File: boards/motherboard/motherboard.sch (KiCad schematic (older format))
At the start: 40 parts, among them J1 RJ45, J2 RJ45, J3 RJ45, J4 RJ45, J5 RJ45, U1 EBAYPCA9685

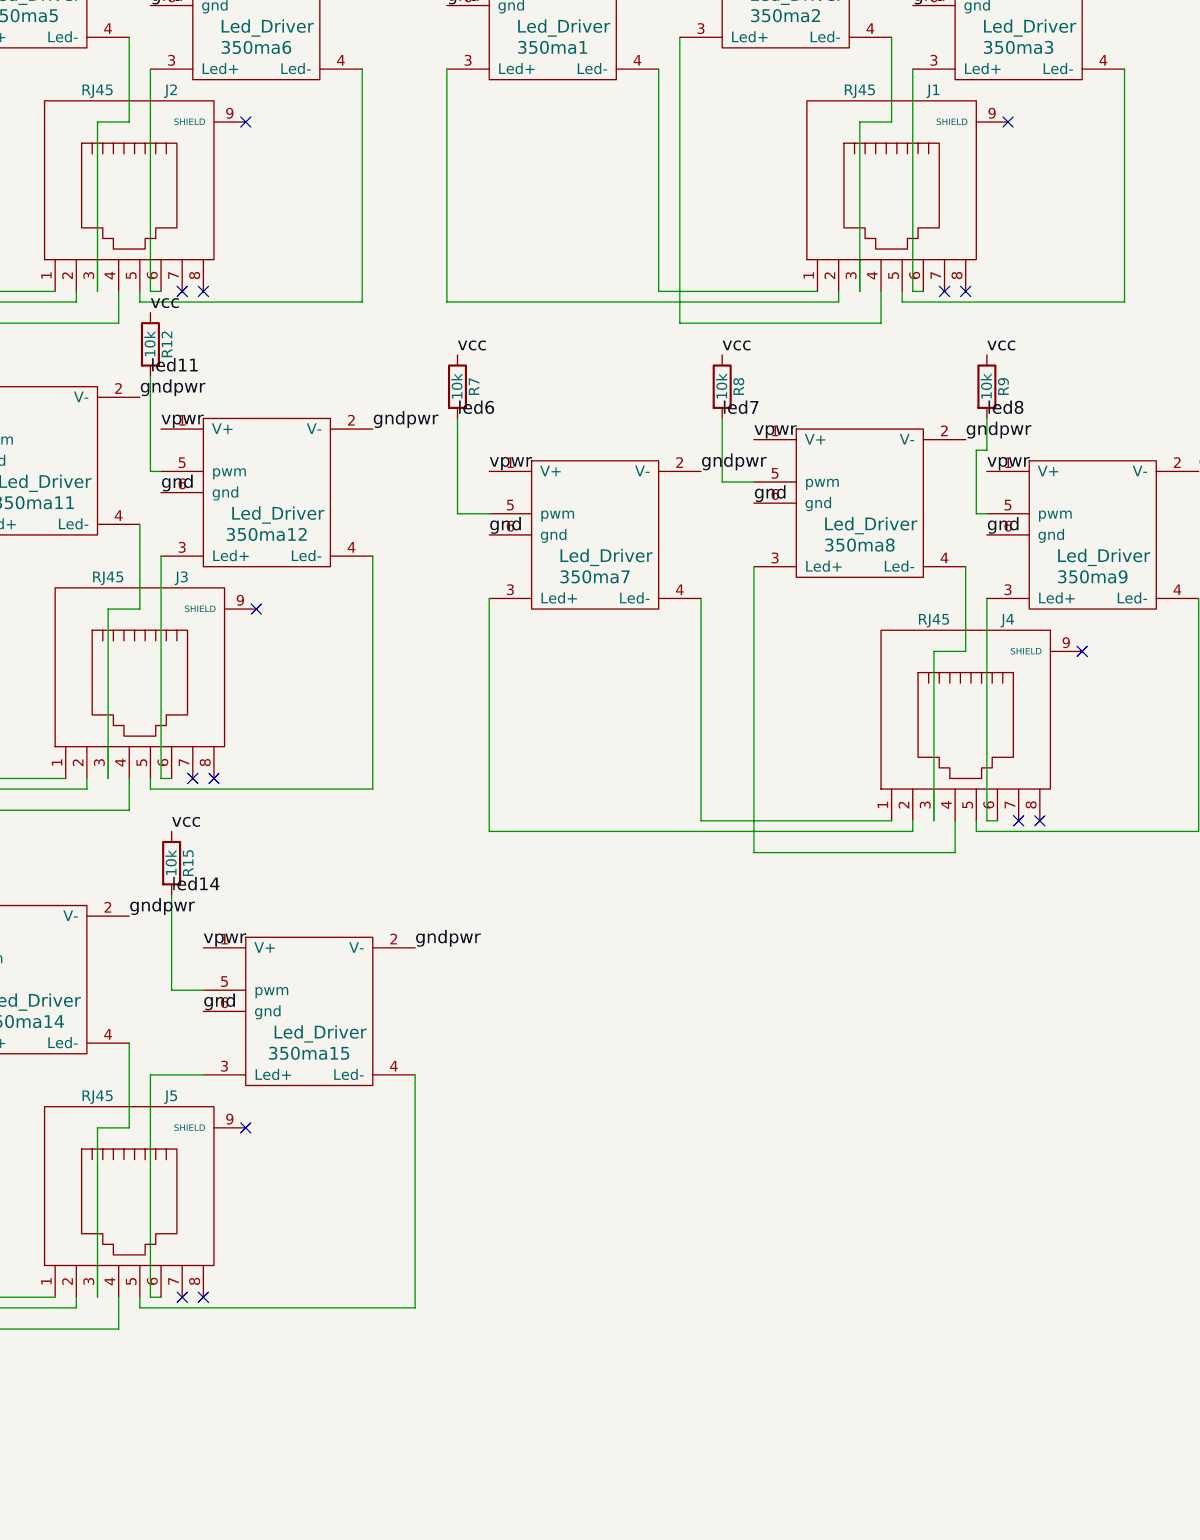
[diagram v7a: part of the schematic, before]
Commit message: added breakout for ethernet
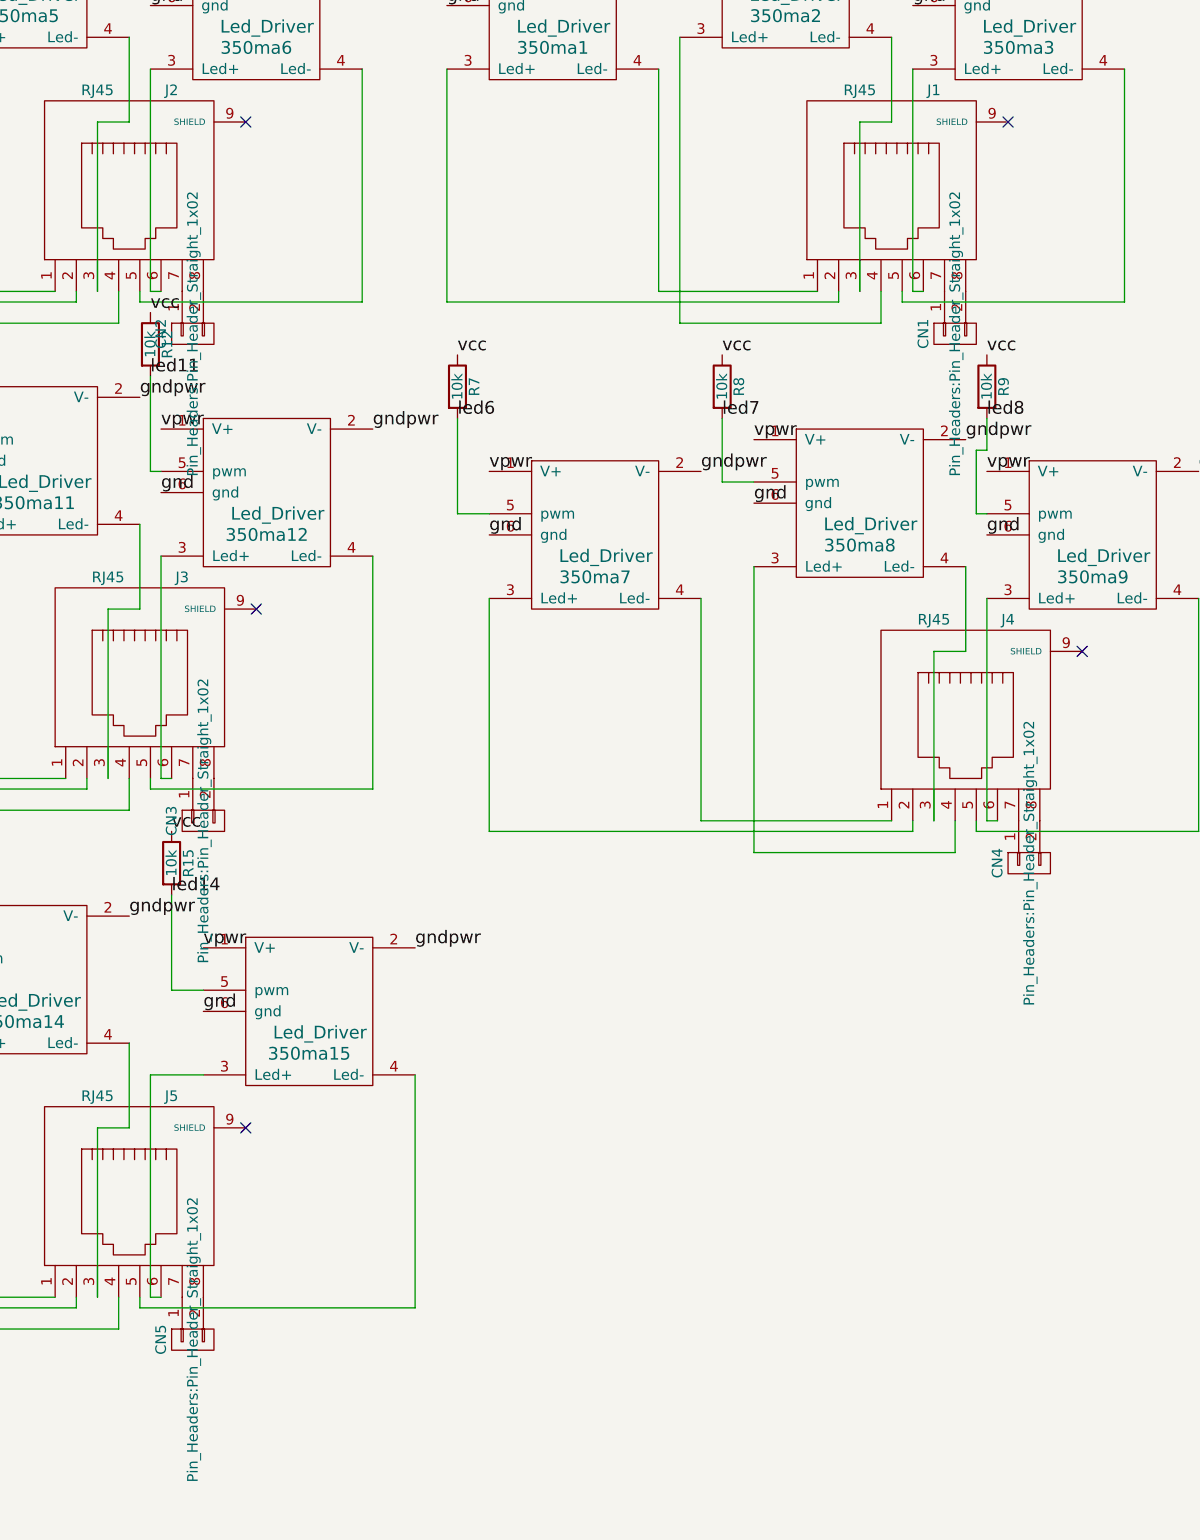
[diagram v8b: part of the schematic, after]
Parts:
- added CN1, CN2, CN3, CN4, CN5: CONN_01X02, Pin_Headers:Pin_Header_Straight_1x02, symbol CONN_01X02
- U1: footprint lighting:pwm_pca9685 -> (none)
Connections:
- net at J1.7: now also CN1.1 (P1)
- net at J1.8: now also CN1.2 (P2)
- net at J4.7: now also CN4.1 (P1)
- net at J4.8: now also CN4.2 (P2)
- net at J2.7: now also CN2.1 (P1)
- net at J2.8: now also CN2.2 (P2)
- net at J3.7: now also CN3.1 (P1)
- net at J3.8: now also CN3.2 (P2)
- net at J5.7: now also CN5.1 (P1)
- net at J5.8: now also CN5.2 (P2)
- no-connect marks 18 -> 8
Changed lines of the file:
@@
 $EndDescr
-$Comp
-L EBAYPCA9685 U1
-U 1 1 5787E341
-P 9550 2750
-F 0 "U1" H 9550 2600 60  0000 C CNN
-F 1 "EBAYPCA9685" H 9550 2850 60  0000 C CNN
-F 2 "lighting:pwm_pca9685" H 9550 2600 60  0001 C CNN
-F 3 "" H 9550 2600 60  0000 C CNN
-	1    9550 2750
-	1    0    0    -1
-$EndComp
 $Comp
 L +24V #PWR01
@@
 NoConn ~ 7200 2050
 NoConn ~ 3600 2050
-NoConn ~ 3300 2850
-NoConn ~ 3400 2850
-NoConn ~ 6900 2850
-NoConn ~ 7000 2850
 Text Label 4200 3500 0    60   ~ 0
 gndpwr
 NoConn ~ 3650 4350
 NoConn ~ 7550 4550
-NoConn ~ 7250 5350
-NoConn ~ 7350 5350
-NoConn ~ 3350 5150
-NoConn ~ 3450 5150
 NoConn ~ 3600 6800
-NoConn ~ 3300 7600
-NoConn ~ 3400 7600
 $Comp
 L GND #PWR03
@@
 Text Label 10550 1250 0    60   ~ 0
 gndpwr
+$Comp
+L CONN_01X02 CN1
+U 1 1 5791F965
+P 6950 3050
+F 0 "CN1" H 6950 3200 50  0000 C CNN
+F 1 "CONN_01X02" V 7050 3050 50  0001 C CNN
+F 2 "Pin_Headers:Pin_Header_Straight_1x02" H 6950 3050 50  0000 C CNN
+F 3 "" H 6950 3050 50  0000 C CNN
+	1    6950 3050
+	0    -1   1    0
+$EndComp
+$Comp
+L CONN_01X02 CN2
+U 1 1 57920C53
+P 3350 3050
+F 0 "CN2" H 3350 3200 50  0000 C CNN
+F 1 "CONN_01X02" V 3450 3050 50  0001 C CNN
+F 2 "Pin_Headers:Pin_Header_Straight_1x02" H 3350 3050 50  0000 C CNN
+F 3 "" H 3350 3050 50  0000 C CNN
+	1    3350 3050
+	0    -1   1    0
+$EndComp
+$Comp
+L CONN_01X02 CN4
+U 1 1 5792107E
+P 7300 5550
+F 0 "CN4" H 7300 5700 50  0000 C CNN
+F 1 "CONN_01X02" V 7400 5550 50  0001 C CNN
+F 2 "Pin_Headers:Pin_Header_Straight_1x02" H 7300 5550 50  0000 C CNN
+F 3 "" H 7300 5550 50  0000 C CNN
+	1    7300 5550
+	0    -1   1    0
+$EndComp
+$Comp
+L CONN_01X02 CN3
+U 1 1 5792142A
+P 3400 5350
+F 0 "CN3" H 3400 5500 50  0000 C CNN
+F 1 "CONN_01X02" V 3500 5350 50  0001 C CNN
+F 2 "Pin_Headers:Pin_Header_Straight_1x02" H 3400 5350 50  0000 C CNN
+F 3 "" H 3400 5350 50  0000 C CNN
+	1    3400 5350
+	0    -1   1    0
+$EndComp
+$Comp
+L CONN_01X02 CN5
+U 1 1 579214D0
+P 3350 7800
+F 0 "CN5" H 3350 7950 50  0000 C CNN
+F 1 "CONN_01X02" V 3450 7800 50  0001 C CNN
+F 2 "Pin_Headers:Pin_Header_Straight_1x02" H 3350 7800 50  0000 C CNN
+F 3 "" H 3350 7800 50  0000 C CNN
+	1    3350 7800
+	0    -1   1    0
+$EndComp
+$Comp
+L EBAYPCA9685 U1
+U 1 1 57922679
+P 9550 2750
+F 0 "U1" H 9550 2600 60  0000 C CNN
+F 1 "EBAYPCA9685" H 9550 2850 60  0000 C CNN
+F 2 "" H 9550 2600 60  0000 C CNN
+F 3 "" H 9550 2600 60  0000 C CNN
+	1    9550 2750
+	1    0    0    -1
+$EndComp
 $EndSCHEMATC
